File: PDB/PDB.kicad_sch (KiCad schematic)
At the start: 2 parts, among them U1 Anderson_Horizontal

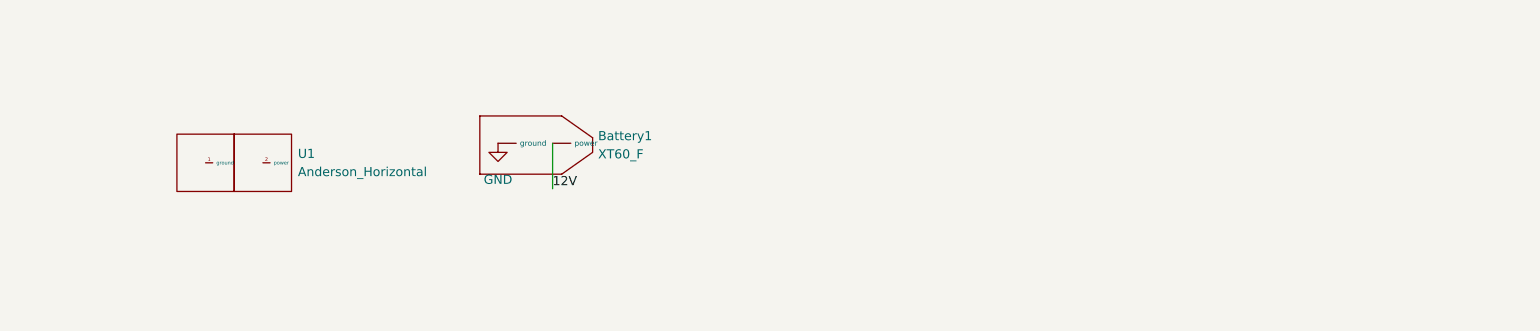
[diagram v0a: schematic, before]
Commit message: Put andersons on PCB, decoup cap needs footprint
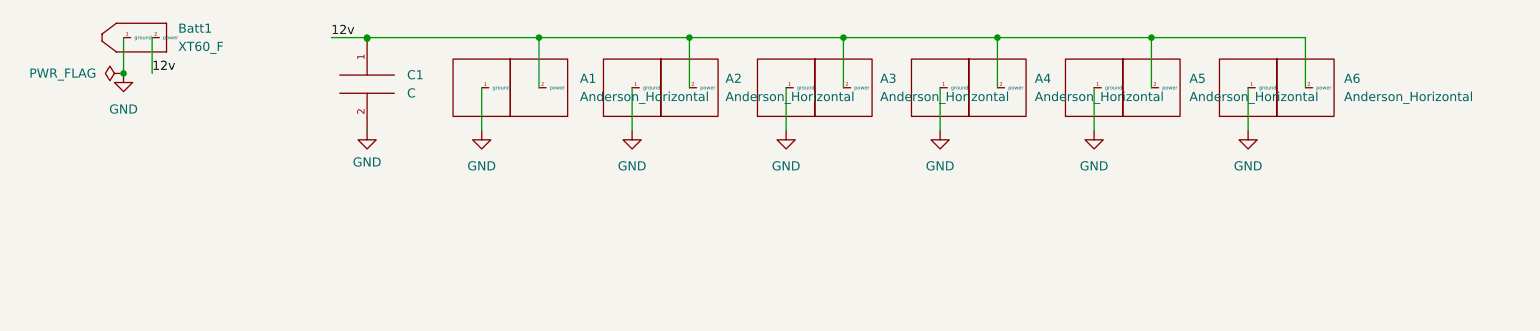
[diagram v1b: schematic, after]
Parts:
- removed Battery1: XT60_F, symbol PiE_Symbols:XT60_F
- added A2, A3, A4, A5, A6: Anderson_Horizontal, PiE_Footprints:anderson_horizontal, symbol PiE_Symbols:Anderson_Horizontal
- added Batt1: XT60_F, PiE_Footprints:XT60_F, symbol PiE_Symbols:XT60_F
- added C1: C, symbol pspice:C
- renumbered U1 to A1
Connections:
- net GND: now also A1.1 (ground), A2.1 (ground), A3.1 (ground), A4.1 (ground), A5.1 (ground), A6.1 (ground), Batt1.1 (ground), C1.2
- net 12v: now reaches A1.2 (power)
- net 12v: now also A2.2 (power), A3.2 (power), A4.2 (power), A5.2 (power), A6.2 (power), Batt1.2 (power), C1.1
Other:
- company: (none) -> Pioneers in Engineering
- title: (none) -> Power Distribution Board
- moved on the sheet: A1

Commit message: added footprint to de cap
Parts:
- C1: footprint (none) -> Capacitor_SMD:C_0603_1608Metric
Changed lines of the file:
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@@
       (effects (font (size 1.27 1.27)) (justify left))
     )
-    (property "Footprint" "" (id 2) (at 63 23.5 0)
+    (property "Footprint" "Capacitor_SMD:C_0603_1608Metric" (id 2) (at 63 23.5 0)
       (effects (font (size 1.27 1.27)) hide)
     )
@@
     )
     (path "/f1dbef02-4e2e-4339-86bb-12922133b71d"
-      (reference "C1") (unit 1) (value "C") (footprint "")
+      (reference "C1") (unit 1) (value "C") (footprint "Capacitor_SMD:C_0603_1608Metric")
     )
   )

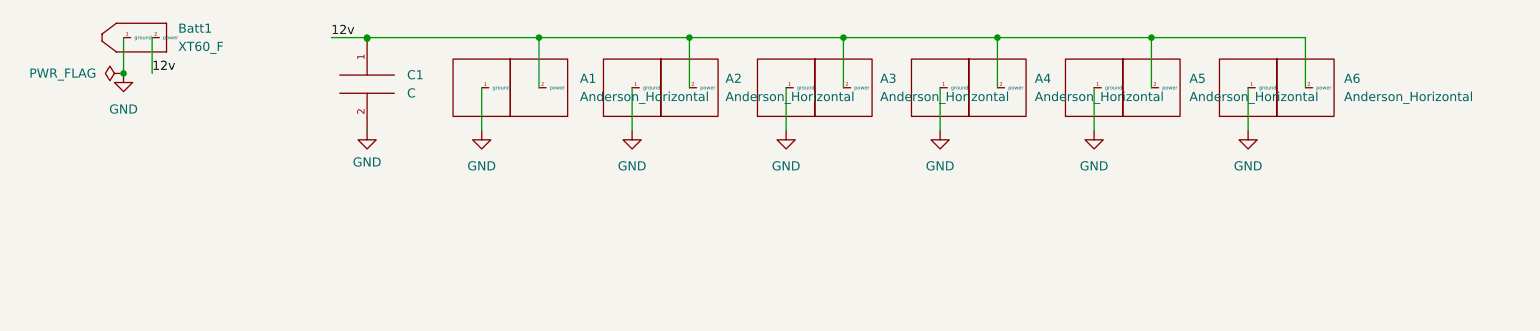
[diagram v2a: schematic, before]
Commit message: added 5v rail and molex connectors
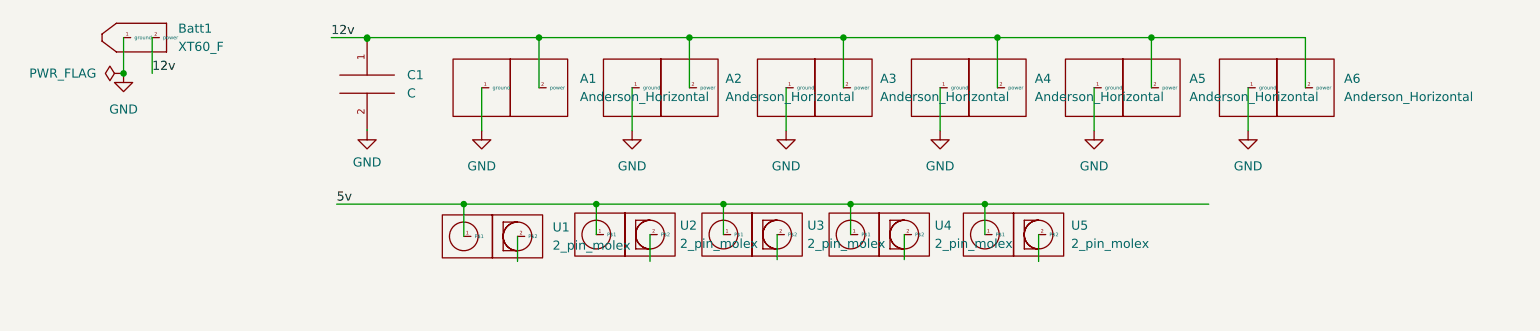
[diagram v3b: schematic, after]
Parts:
- added U1, U2, U3, U4, U5: 2_pin_molex, PiE_Footprints:ATX, symbol PiE_Symbols:2_pin_molex
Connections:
- new net 5v: U1.1 (P$1), U2.1 (P$1), U3.1 (P$1), U4.1 (P$1), U5.1 (P$1)
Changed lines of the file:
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@@
   (junction (at 129.5 17) (diameter 0) (color 0 0 0 0)
   )
+  (junction (at 76.5 40.25) (diameter 0) (color 0 0 0 0)
+  )
+  (junction (at 149.25 40.25) (diameter 0) (color 0 0 0 0)
+  )
   (junction (at 108 17) (diameter 0) (color 0 0 0 0)
   )
   (junction (at 151 17) (diameter 0) (color 0 0 0 0)
   )
+  (junction (at 95 40.25) (diameter 0) (color 0 0 0 0)
+  )
   (junction (at 29 22) (diameter 0) (color 0 0 0 0)
   )
   (junction (at 63 17.15) (diameter 0) (color 0 0 0 0)
   )
+  (junction (at 112.75 40.25) (diameter 0) (color 0 0 0 0)
+  )
   (junction (at 172.5 17) (diameter 0) (color 0 0 0 0)
   )
+  (junction (at 130.5 40.25) (diameter 0) (color 0 0 0 0)
+  )
   (wire (pts (xy 58 17) (xy 63 17))
     (stroke (width 0) (type default) (color 0 0 0 0))
@@
     (stroke (width 0) (type default) (color 0 0 0 0))
   )
+  (wire (pts (xy 130.5 40.25) (xy 130.5 44.5))
+    (stroke (width 0) (type default) (color 0 0 0 0))
+  )
   (wire (pts (xy 87 17) (xy 87 24))
     (stroke (width 0) (type default) (color 0 0 0 0))
@@
     (stroke (width 0) (type default) (color 0 0 0 0))
   )
+  (wire (pts (xy 58.75 40.25) (xy 76.5 40.25))
+    (stroke (width 0) (type default) (color 0 0 0 0))
+  )
   (wire (pts (xy 63 17.15) (xy 63 17))
     (stroke (width 0) (type default) (color 0 0 0 0))
   )
+  (wire (pts (xy 76.5 40.25) (xy 95 40.25))
+    (stroke (width 0) (type default) (color 0 0 0 0))
+  )
   (wire (pts (xy 186 24) (xy 186 30))
     (stroke (width 0) (type default) (color 0 0 0 0))
@@
     (stroke (width 0) (type default) (color 0 0 0 0))
   )
+  (wire (pts (xy 149.25 40.25) (xy 180.5 40.25))
+    (stroke (width 0) (type default) (color 0 0 0 0))
+  )
   (wire (pts (xy 194 17) (xy 194 24))
     (stroke (width 0) (type default) (color 0 0 0 0))
   )
+  (wire (pts (xy 138 44.5) (xy 138 48))
+    (stroke (width 0) (type default) (color 0 0 0 0))
+  )
   (wire (pts (xy 129.5 17) (xy 129.5 24))
     (stroke (width 0) (type default) (color 0 0 0 0))
@@
     (stroke (width 0) (type default) (color 0 0 0 0))
   )
+  (wire (pts (xy 84 44.75) (xy 84 48.25))
+    (stroke (width 0) (type default) (color 0 0 0 0))
+  )
   (wire (pts (xy 121.5 24) (xy 121.5 30))
     (stroke (width 0) (type default) (color 0 0 0 0))
@@
     (stroke (width 0) (type default) (color 0 0 0 0))
   )
+  (wire (pts (xy 149.25 40.25) (xy 149.25 44.5))
+    (stroke (width 0) (type default) (color 0 0 0 0))
+  )
   (wire (pts (xy 151 17) (xy 151 24))
     (stroke (width 0) (type default) (color 0 0 0 0))
   )
+  (wire (pts (xy 112.75 40.25) (xy 130.5 40.25))
+    (stroke (width 0) (type default) (color 0 0 0 0))
+  )
+  (wire (pts (xy 76.5 40.25) (xy 76.5 44.75))
+    (stroke (width 0) (type default) (color 0 0 0 0))
+  )
+  (wire (pts (xy 156.75 44.5) (xy 156.75 48.25))
+    (stroke (width 0) (type default) (color 0 0 0 0))
+  )
+  (wire (pts (xy 102.5 44.5) (xy 102.5 48.25))
+    (stroke (width 0) (type default) (color 0 0 0 0))
+  )
   (wire (pts (xy 100 24) (xy 100 30))
     (stroke (width 0) (type default) (color 0 0 0 0))
@@
     (stroke (width 0) (type default) (color 0 0 0 0))
   )
+  (wire (pts (xy 95 40.25) (xy 112.75 40.25))
+    (stroke (width 0) (type default) (color 0 0 0 0))
+  )
+  (wire (pts (xy 95 40.25) (xy 95 44.5))
+    (stroke (width 0) (type default) (color 0 0 0 0))
+  )
   (wire (pts (xy 63 17) (xy 87 17))
     (stroke (width 0) (type default) (color 0 0 0 0))
@@
     (stroke (width 0) (type default) (color 0 0 0 0))
   )
+  (wire (pts (xy 120.25 44.5) (xy 120.25 48))
+    (stroke (width 0) (type default) (color 0 0 0 0))
+  )
   (wire (pts (xy 143 24) (xy 143 30))
     (stroke (width 0) (type default) (color 0 0 0 0))
+  )
+  (wire (pts (xy 112.75 40.25) (xy 112.75 44.5))
+    (stroke (width 0) (type default) (color 0 0 0 0))
+  )
+  (wire (pts (xy 130.5 40.25) (xy 149.25 40.25))
+    (stroke (width 0) (type default) (color 0 0 0 0))
+  )
+  (label "5v" (at 58.75 40.25 0)
+    (effects (font (size 1.27 1.27)) (justify left bottom))
   )
   (label "12v" (at 58 17 0)
@@
   (label "12v" (at 33 22 0)
     (effects (font (size 1.27 1.27)) (justify left bottom))
+  )
+  (symbol (lib_id "PiE_Symbols:2_pin_molex") (at 116.75 41.5 0) (unit 1)
+    (in_bom yes) (on_board yes) (fields_autoplaced)
+    (property "Reference" "U3" (id 0) (at 124.46 43.2299 0)
+      (effects (font (size 1.27 1.27)) (justify left))
+    )
+    (property "Value" "2_pin_molex" (id 1) (at 124.46 45.7699 0)
+      (effects (font (size 1.27 1.27)) (justify left))
+    )
+    (property "Footprint" "PiE_Footprints:ATX" (id 2) (at 116.75 41.5 0)
+      (effects (font (size 1.27 1.27)) hide)
+    )
+    (property "Datasheet" "" (id 3) (at 116.75 41.5 0)
+      (effects (font (size 1.27 1.27)) hide)
+    )
+    (pin "1")
+    (pin "2")
+  )
+  (symbol (lib_id "PiE_Symbols:2_pin_molex") (at 153.25 41.5 0) (unit 1)
+    (in_bom yes) (on_board yes) (fields_autoplaced)
+    (property "Reference" "U5" (id 0) (at 161.29 43.2299 0)
+      (effects (font (size 1.27 1.27)) (justify left))
+    )
+    (property "Value" "2_pin_molex" (id 1) (at 161.29 45.7699 0)
+      (effects (font (size 1.27 1.27)) (justify left))
+    )
+    (property "Footprint" "PiE_Footprints:ATX" (id 2) (at 153.25 41.5 0)
+      (effects (font (size 1.27 1.27)) hide)
+    )
+    (property "Datasheet" "" (id 3) (at 153.25 41.5 0)
+      (effects (font (size 1.27 1.27)) hide)
+    )
+    (pin "1")
+    (pin "2")
+  )
+  (symbol (lib_id "PiE_Symbols:2_pin_molex") (at 134.5 41.5 0) (unit 1)
+    (in_bom yes) (on_board yes) (fields_autoplaced)
+    (property "Reference" "U4" (id 0) (at 142.24 43.2299 0)
+      (effects (font (size 1.27 1.27)) (justify left))
+    )
+    (property "Value" "2_pin_molex" (id 1) (at 142.24 45.7699 0)
+      (effects (font (size 1.27 1.27)) (justify left))
+    )
+    (property "Footprint" "PiE_Footprints:ATX" (id 2) (at 134.5 41.5 0)
+      (effects (font (size 1.27 1.27)) hide)
+    )
+    (property "Datasheet" "" (id 3) (at 134.5 41.5 0)
+      (effects (font (size 1.27 1.27)) hide)
+    )
+    (pin "1")
+    (pin "2")
   )
   (symbol (lib_id "PiE_Symbols:Anderson_Horizontal") (at 190 20 0) (unit 1)
@@
     (pin "1")
   )
+  (symbol (lib_id "PiE_Symbols:2_pin_molex") (at 80.5 41.75 0) (unit 1)
+    (in_bom yes) (on_board yes) (fields_autoplaced)
+    (property "Reference" "U1" (id 0) (at 88.9 43.4799 0)
+      (effects (font (size 1.27 1.27)) (justify left))
+    )
+    (property "Value" "2_pin_molex" (id 1) (at 88.9 46.0199 0)
+      (effects (font (size 1.27 1.27)) (justify left))
+    )
+    (property "Footprint" "PiE_Footprints:ATX" (id 2) (at 80.5 41.75 0)
+      (effects (font (size 1.27 1.27)) hide)
+    )
+    (property "Datasheet" "" (id 3) (at 80.5 41.75 0)
+      (effects (font (size 1.27 1.27)) hide)
+    )
+    (pin "1")
+    (pin "2")
+  )
   (symbol (lib_id "PiE_Symbols:Anderson_Horizontal") (at 168.5 20 0) (unit 1)
     (in_bom yes) (on_board yes) (fields_autoplaced)
@@
     )
     (pin "1")
+  )
+  (symbol (lib_id "PiE_Symbols:2_pin_molex") (at 99 41.5 0) (unit 1)
+    (in_bom yes) (on_board yes) (fields_autoplaced)
+    (property "Reference" "U2" (id 0) (at 106.68 43.2299 0)
+      (effects (font (size 1.27 1.27)) (justify left))
+    )
+    (property "Value" "2_pin_molex" (id 1) (at 106.68 45.7699 0)
+      (effects (font (size 1.27 1.27)) (justify left))
+    )
+    (property "Footprint" "PiE_Footprints:ATX" (id 2) (at 99 41.5 0)
+      (effects (font (size 1.27 1.27)) hide)
+    )
+    (property "Datasheet" "" (id 3) (at 99 41.5 0)
+      (effects (font (size 1.27 1.27)) hide)
+    )
+    (pin "1")
+    (pin "2")
   )
   (symbol (lib_id "power:GND") (at 143 30 0) (unit 1)
@@
       (reference "C1") (unit 1) (value "C") (footprint "Capacitor_SMD:C_0603_1608Metric")
     )
-  )
+    (path "/531ec580-330f-4072-9d5d-cefad53c05ad"
+      (reference "U1") (unit 1) (value "2_pin_molex") (footprint "PiE_Footprints:ATX")
+    )
+    (path "/9b396cc9-f41a-4fb2-85f2-864cfecee26f"
+      (reference "U2") (unit 1) (value "2_pin_molex") (footprint "PiE_Footprints:ATX")
+    )
+    (path "/09d74e85-a027-471b-ba33-5b0f621da0ec"
+      (reference "U3") (unit 1) (value "2_pin_molex") (footprint "PiE_Footprints:ATX")
+    )
+    (path "/152130a7-6827-411f-b933-285f49ef42a0"
+      (reference "U4") (unit 1) (value "2_pin_molex") (footprint "PiE_Footprints:ATX")
+    )
+    (path "/0a1e9669-8f9a-4f81-ad2a-4f3c74dc6627"
+      (reference "U5") (unit 1) (value "2_pin_molex") (footprint "PiE_Footprints:ATX")
+    )
+  )

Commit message: added Converter symbol/footprint
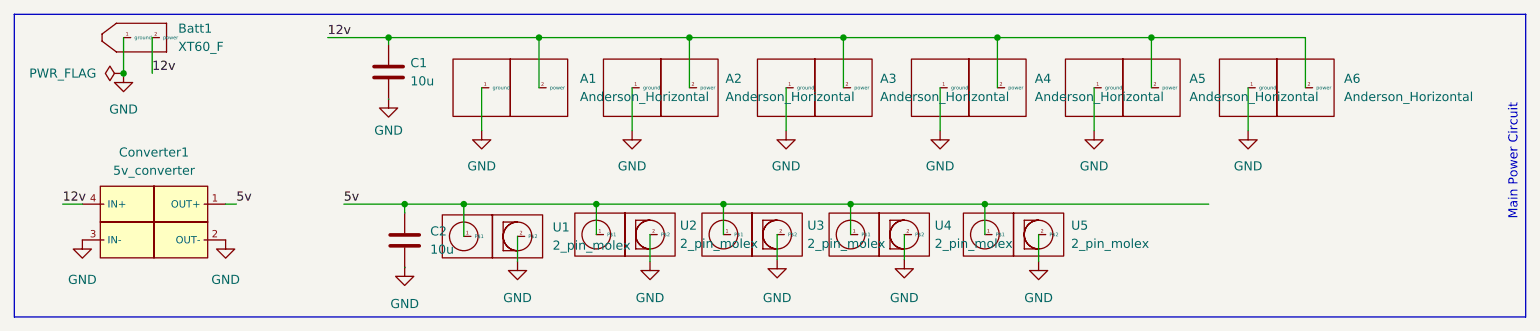
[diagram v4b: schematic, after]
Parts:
- removed C1: C, Capacitor_SMD:C_0603_1608Metric, symbol pspice:C
- added C1, C2: 10u, Capacitor_SMD:C_0805_2012Metric, symbol Device:C
- added Converter1: 5v_converter, PiE_Footprints:5v_converter, symbol PiE_Symbols:5v_converter
- U1, U2, U3, U4, U5: footprint PiE_Footprints:ATX -> PiE_Footprints:2_pin_molex
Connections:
- net 12v: now also C1.1, Converter1.4 (IN+)
- net 5v: now also C2.1, Converter1.1 (OUT+)
- net GND: now also U1.2 (P$2), U2.2 (P$2), U3.2 (P$2), U4.2 (P$2), U5.2 (P$2), C1.2, C2.2, Converter1.2 (OUT-), Converter1.3 (IN-)
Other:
- note added: "Main Power Circuit"
